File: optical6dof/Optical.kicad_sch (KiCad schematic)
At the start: 24 parts, among them Q1 Q_Photo_NPN, Q2 Q_Photo_NPN, Q3 Q_Photo_NPN, Q4 Q_Photo_NPN, Q5 Q_Photo_NPN, Q6 Q_Photo_NPN

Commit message: merged repos
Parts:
- removed Q1, Q2, Q3, Q4, Q5, Q6: Q_Photo_NPN, symbol Device:Q_Photo_NPN
- added Q1, Q2, Q3: ~, library:0603_sidemount, symbol library:dual_phototransistor
- added U1: MAX11617EWE+T, library:21-0491G_W162E2-1_MXM, symbol MAX11617EWE:MAX11617EWE+T
- D1, D2, D3: footprint (none) -> LED_SMD:LED_0402_1005Metric; Digikey (none) -> https://www.inolux-corp.com/datasheet/IR/Emitter/940%20nm%2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
- R1, R2, R3, R4, R5, R6: value 3K -> 1.5k; footprint Resistor_SMD:R_0201_0603Metric -> Resistor_SMD:R_01005_0402Metric; Digikey (none) -> https://www.digikey.com/en/products/detail/delta-electronic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
- R7, R8, R9: value 1K -> 200r; footprint Resistor_SMD:R_0201_0603Metric -> Resistor_SMD:R_01005_0402Metric; Digikey (none) -> https://www.digikey.com/en/products/detail/yageo/RC0100FR-0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
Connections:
- net A1: now also Q1.2 (E)
- net A2: now also Q1.3 (E)
- net B1: now also Q2.2 (E)
- net B2: now also Q2.3 (E)
- net C1: now also Q3.2 (E)
- net C2: now also Q3.3 (E)
- net GND: now also U1.D1 (GND)
- net VDD: now also Q1.1 (C), Q2.1 (C), Q3.1 (C), U1.C1 (VDD)
- new net SCL: U1.D2 (SCL)
- new net SDA: U1.D3 (SDA)
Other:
- note added: "3.3v/2.42mA"
- note added: "Ic(on) = 2.42mA max"
- note removed: "MAX11617EWE"
- moved on the sheet: R1, R2, R3, R4, R5, R6, TP1, TP2, TP3, TP4, TP5, TP6

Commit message: routed the pcb
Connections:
- net A1: now also U1.A1 (AIN0)
- net A2: now also U1.B1 (AIN9)
- net B1: now also U1.A4 (AIN3)
- net B2: now also U1.A2 (AIN1)
- net C1: now also U1.C4 (AIN5)
- net C2: now also U1.B4 (AIN4)
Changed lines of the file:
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@@
+		)
+	)
+	(label "B2"
+		(at 104.775 149.86 180)
+		(effects
+			(font
+				(size 1.27 1.27)
+			)
+			(justify right bottom)
 		)
 	)
@@
 		)
 	)
+	(label "B1"
+		(at 104.775 154.94 180)
+		(effects
+			(font
+				(size 1.27 1.27)
+			)
+			(justify right bottom)
+		)
+	)
 	(label "B2"
 		(at 106.045 104.14 180)
@@
 		)
 	)
+	(label "A1"
+		(at 104.775 147.32 180)
+		(effects
+			(font
+				(size 1.27 1.27)
+			)
+			(justify right bottom)
+		)
+	)
+	(label "C1"
+		(at 141.605 157.48 0)
+		(effects
+			(font
+				(size 1.27 1.27)
+			)
+			(justify left bottom)
+		)
+	)
 	(label "A2"
 		(at 51.435 104.14 180)
+		(effects
+			(font
+				(size 1.27 1.27)
+			)
+			(justify right bottom)
+		)
+	)
+	(label "A2"
+		(at 104.775 157.48 180)
 		(effects
 			(font
@@
 		)
 	)
+	(label "C2"
+		(at 104.775 165.1 180)
+		(effects
+			(font
+				(size 1.27 1.27)
+			)
+			(justify right bottom)
+		)
+	)

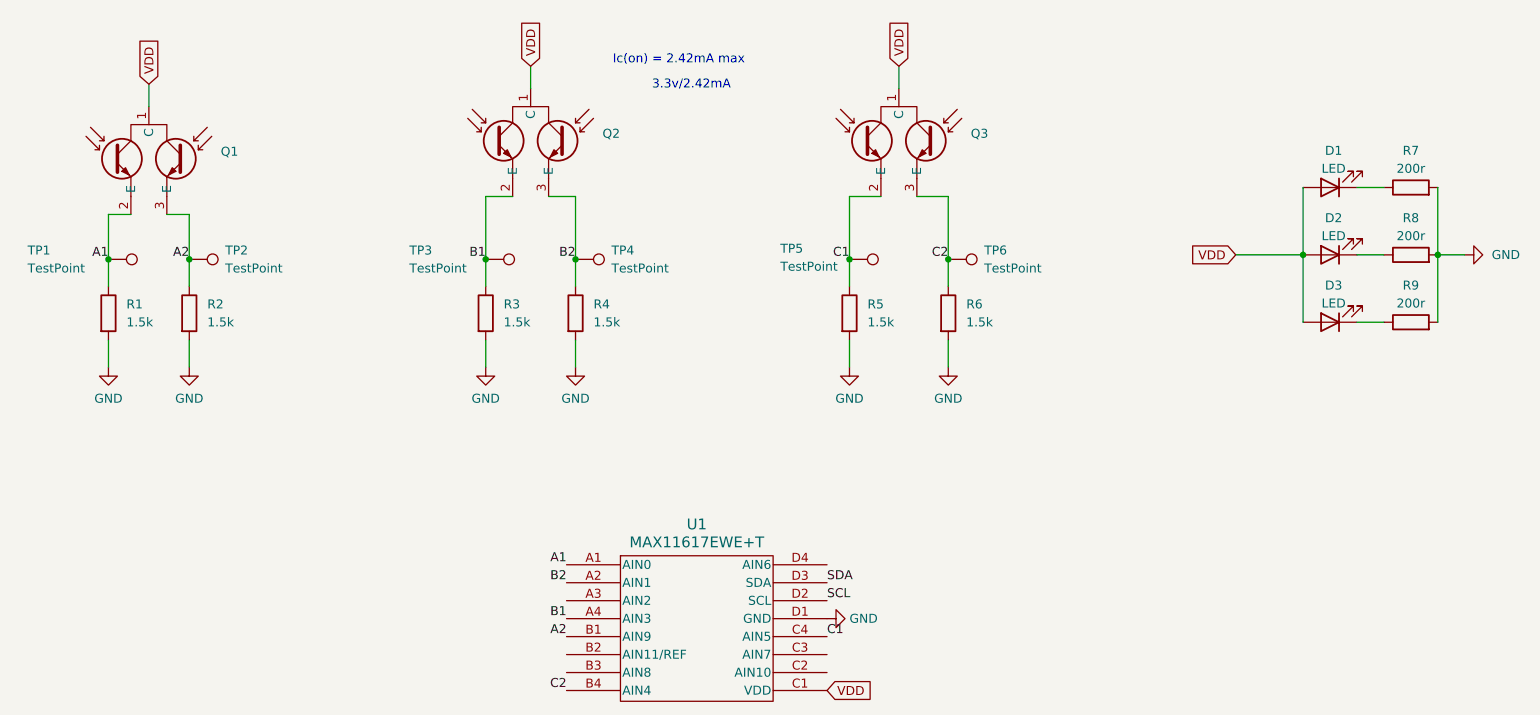
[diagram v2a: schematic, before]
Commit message: layout changes to schematic
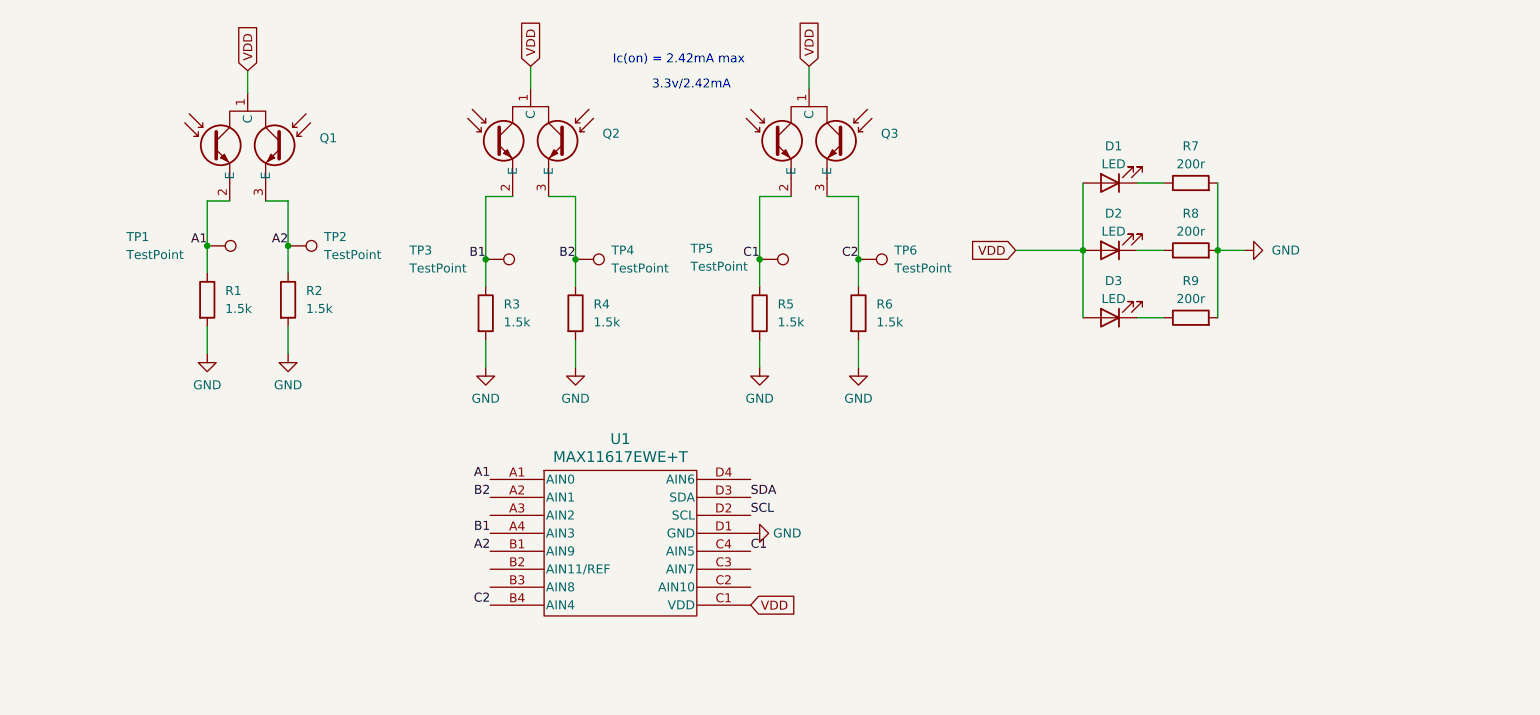
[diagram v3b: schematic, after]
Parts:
- D1, D2, D3: Digikey https://www.inolux-corp.com/datasheet/IR/Emitter/940%20nm%2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 -> https://www.digikey.com/en/products/detail/inolux/IN-S42CTQ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
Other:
- moved on the sheet: D1, D2, D3, Q1, Q3, R1, R2, R5, R6, R7, R8, R9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
